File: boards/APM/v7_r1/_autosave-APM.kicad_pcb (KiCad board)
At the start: 6 copper layers, 72.5 x 111.9 mm, 171 parts, among them J1 DF40C-60DS-0.4V(51), J11 DAC_L_PRB, J12 Conn_01x02, J13 ACM_DAC_L, J16 USB_A_FEMALE, J19 AudioPlug3, J2 AUDIO_PWR, J23 VOL_L_CTRL, J24 VOL_R_CTRL, J3 DF40C-60DS-0.4V(51), J30 UART_DEBUG, J31 Conn_02x04_Odd_Even, J4 LCD_display, J5 Barrel_Jack, J6 OSC_CTRL, J7 DAC_R_PRB, J8 AUDIO_CTRL, J9 ACM_DAC_R, SW1 RST, U11 CS4344, U12 OPA1656ID, U13 INA219AxD, U14 LTC660, U2 OPA1678, U3 LT1963AxST-3.3, U4 W25Q128JVS, U5 MR25H40, U6 W25Q128JVS, U7 INA219AxD, U8 24LC1025-I_P, U9 USBLC6-2SC6

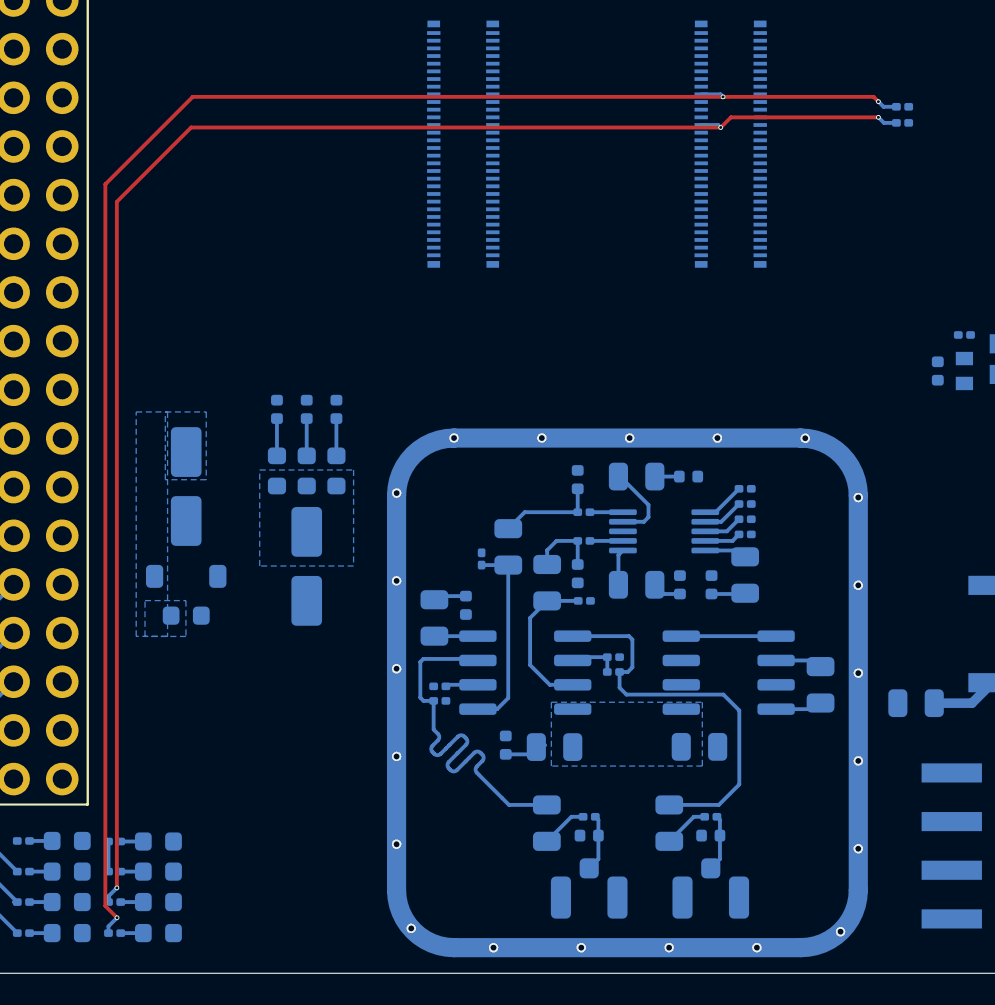
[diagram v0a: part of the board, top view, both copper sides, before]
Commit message: update render. update guard ring
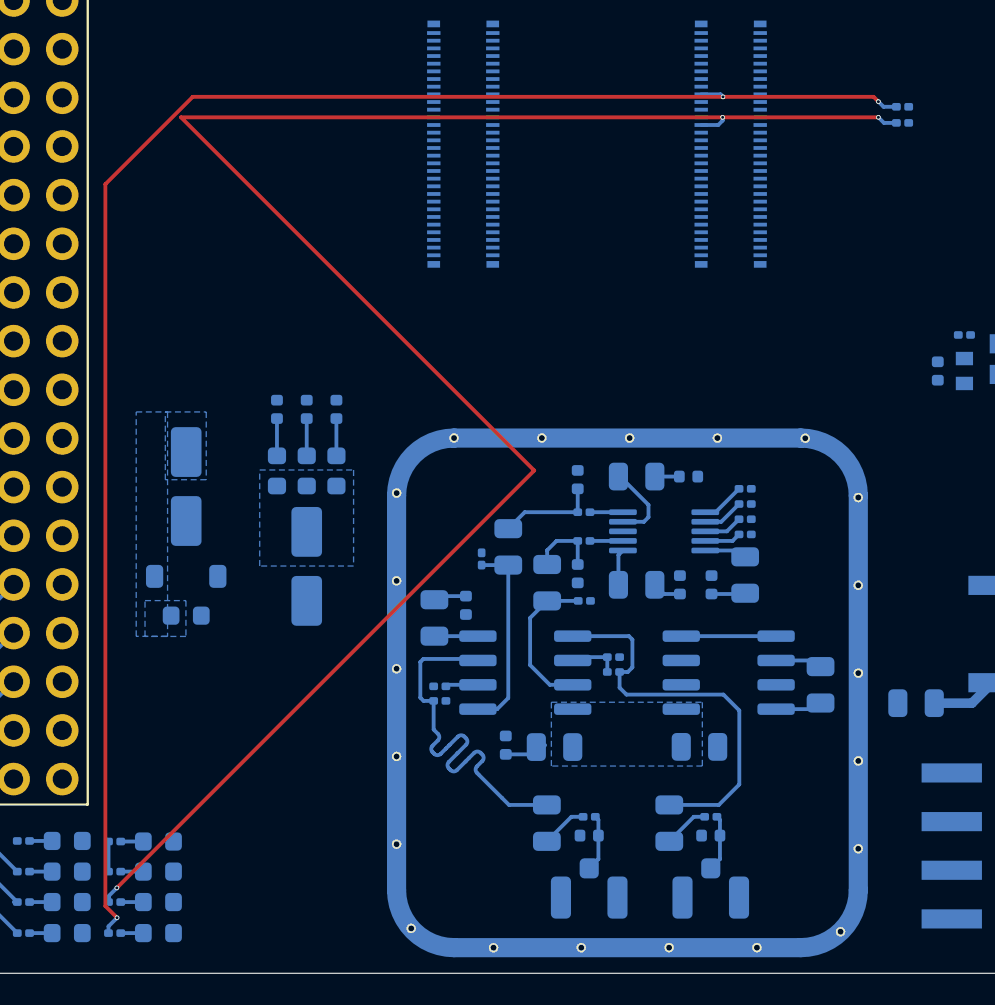
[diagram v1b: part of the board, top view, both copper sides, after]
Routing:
- net /FPGA_INTERFACE/D7_DONE: track 80.5 -> 96.6 mm

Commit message: more placement
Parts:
- moved J11 61.5 mm to (101.0, 82.6), turned to 180 degrees
- moved C2 61.3 mm to (90.1, 72.5)
- moved R43 61.3 mm to (90.7, 91.4)
- moved R45 61.3 mm to (88.6, 91.4)
- moved R46 61.3 mm to (83.3, 91.4)
- moved U2 61.3 mm to (87.0, 80.7)
- moved C13 61.3 mm to (85.4, 89.1)
- moved R44 61.3 mm to (85.4, 91.4)
- moved C10 61.3 mm to (88.6, 89.1)
- moved C11 61.3 mm to (90.7, 89.1)
- moved C12 61.3 mm to (83.3, 89.1)
- moved C3 61.3 mm to (80.6, 77.0)
- moved J12 57.5 mm to (98.8, 78.3), turned to 90 degrees
- moved J7 52.0 mm to (96.1, 82.6), turned to 0 degrees
- moved R7 49.7 mm to (48.0, 75.9)
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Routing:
- net /FPGA_INTERFACE/D7_DONE: track 96.6 -> 80.9 mm
- net ACM_DAC_MCLK: track 0.00 -> 1.20 mm, vias 0 -> 1
- net ACM_DAC_SCLK: track 0.00 -> 1.19 mm, vias 0 -> 1
- net ACM_DAC_LRCK: track 0.00 -> 0.94 mm, vias 0 -> 1
- net ACM_DAC_SDIN: track 0.00 -> 0.93 mm, vias 0 -> 1
